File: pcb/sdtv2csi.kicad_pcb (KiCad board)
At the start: 2 copper layers, 25 x 40 mm, 67 parts, among them J1 VIDEO_IN, J2 RPI_CSI_TOP, U1 ADV7280A-M, U2 NJM12888F18, Y1 ABM8G-28.63636MHZ

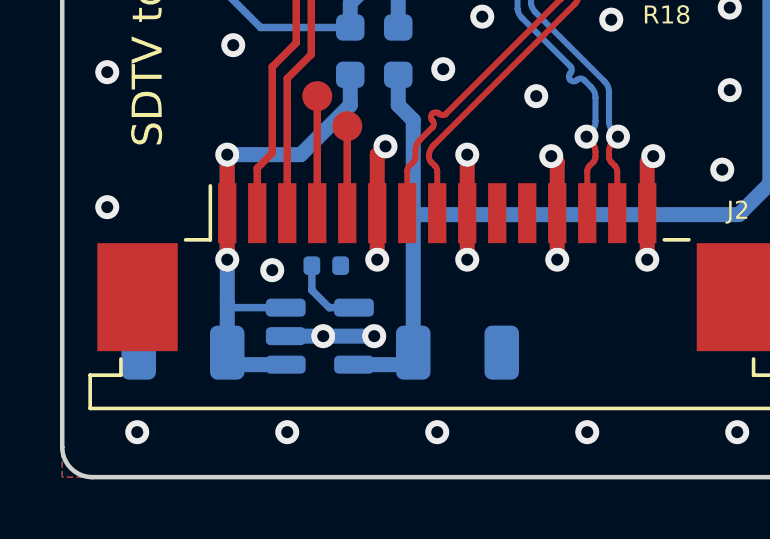
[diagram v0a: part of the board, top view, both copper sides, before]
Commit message: Replacement of NJM12888F18 to TLV70218QDBVRQ1
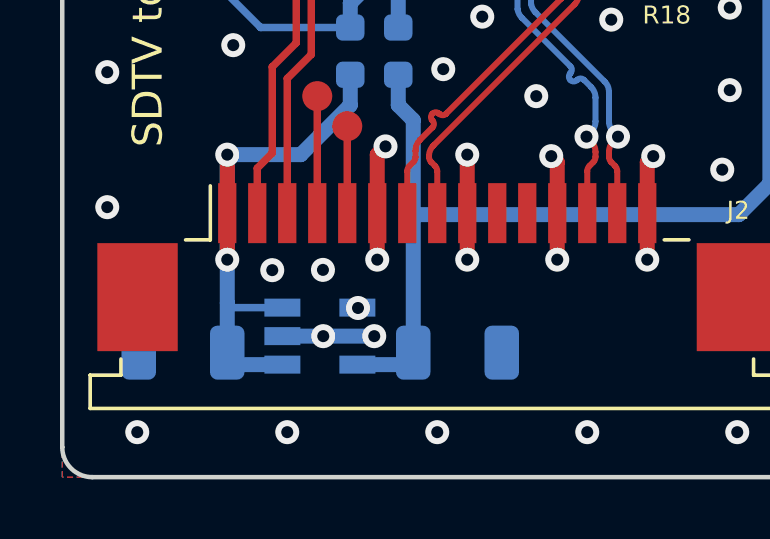
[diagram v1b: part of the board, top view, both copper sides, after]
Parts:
- removed C14: 10nF, Capacitor_SMD:C_0402_1005Metric
- U2: value NJM12888F18 -> TLV70218QDBVRQ1; footprint Package_TO_SOT_SMD:SOT-23-5 -> Library:SOT95P280X145-5N
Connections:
- U2 pad 4: Net-(C14-Pad1) -> GND
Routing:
- net Net-(C14-Pad1): track 2.47 -> 0.00 mm
- net GND: vias 53 -> 55

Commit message: Update C9 / C10 and change ABM8G
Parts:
- C11, C9: value 20pF -> 10pF
- Y1: value ABM8G-28.63636MHZ -> ABM8G-28.63636MHZ-4Y-T3
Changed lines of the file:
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@@
 			)
 		)
-		(property "Value" "20pF"
+		(property "Value" "10pF"
 			(at 0 1.16 0)
 			(layer "F.Fab")
@@
 			)
 		)
-		(property "Value" "ABM8G-28.63636MHZ"
+		(property "Value" "ABM8G-28.63636MHZ-4Y-T3"
 			(at 0 2.45 90)
 			(layer "F.Fab")
@@
 			)
 		)
-		(property "Value" "20pF"
+		(property "Value" "10pF"
 			(at 0 1.16 90)
 			(layer "F.Fab")

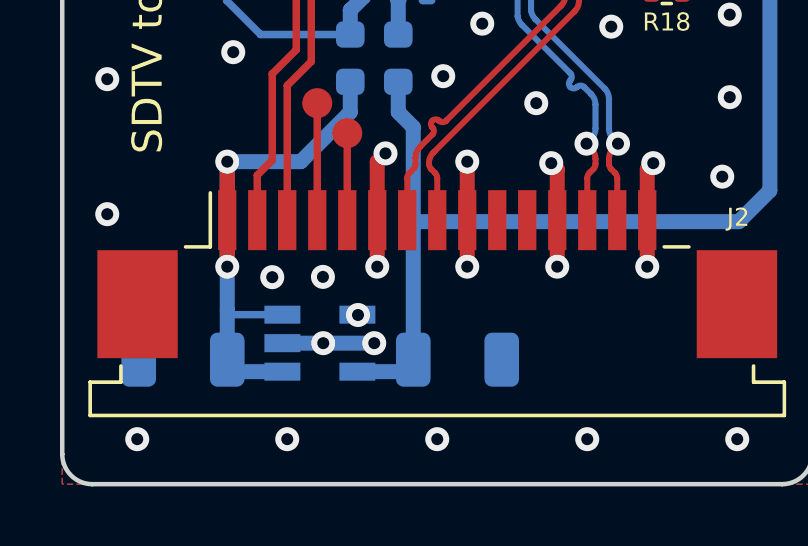
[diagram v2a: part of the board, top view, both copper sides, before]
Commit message: Remove via on NC pad
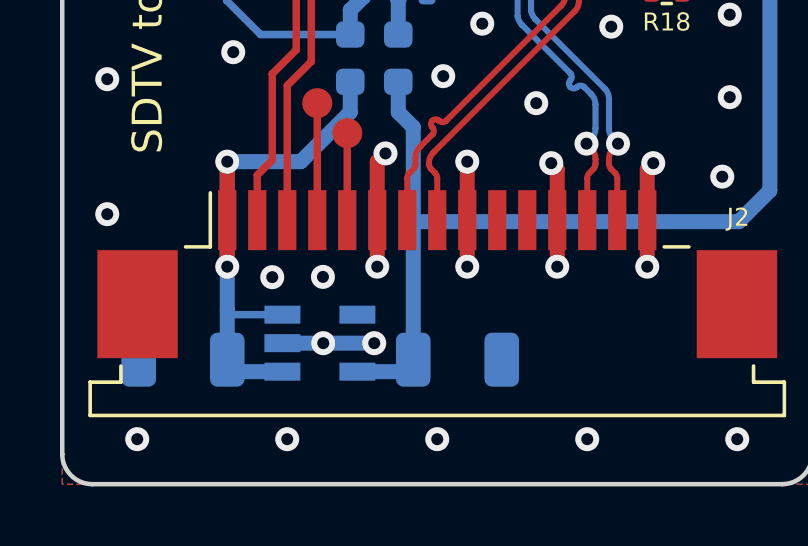
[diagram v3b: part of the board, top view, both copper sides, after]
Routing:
- net GND: vias 55 -> 54
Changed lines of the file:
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@@
-	)
-	(via
-		(at 59.8584 74.3612)
-		(size 0.8)
-		(drill 0.4)
-		(layers "F.Cu" "B.Cu")
-		(net 1)
 	)
 	(via

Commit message: Cosmetic
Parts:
- added G***: LOGO, Library:coeurlolopetit, B.Cu at (69.2, 75.9)
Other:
- board text added: "Analogue to CSI Converter"
- board text removed: "2022-07"
- board text removed: "SDTV to CSI Video Decoder"
